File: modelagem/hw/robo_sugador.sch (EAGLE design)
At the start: 34 parts, among them M1 Roda esquerda, M2 Roda direita, M3 Sugador, M4 Servo

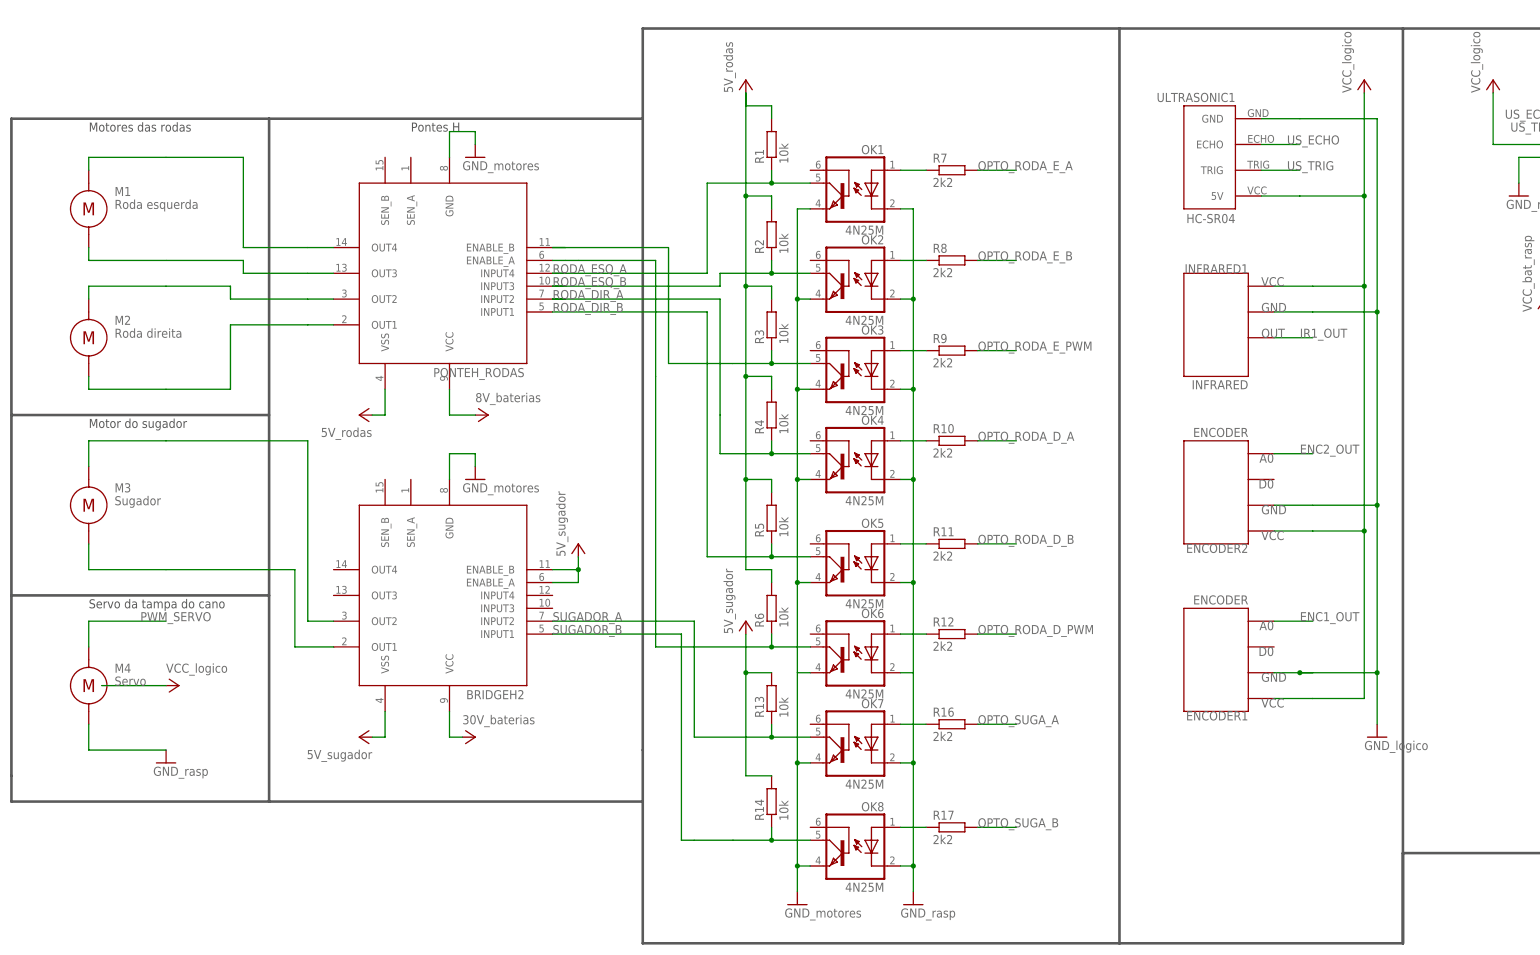
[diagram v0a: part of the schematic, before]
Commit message: Atualiza esquematico de hw e suas figuras
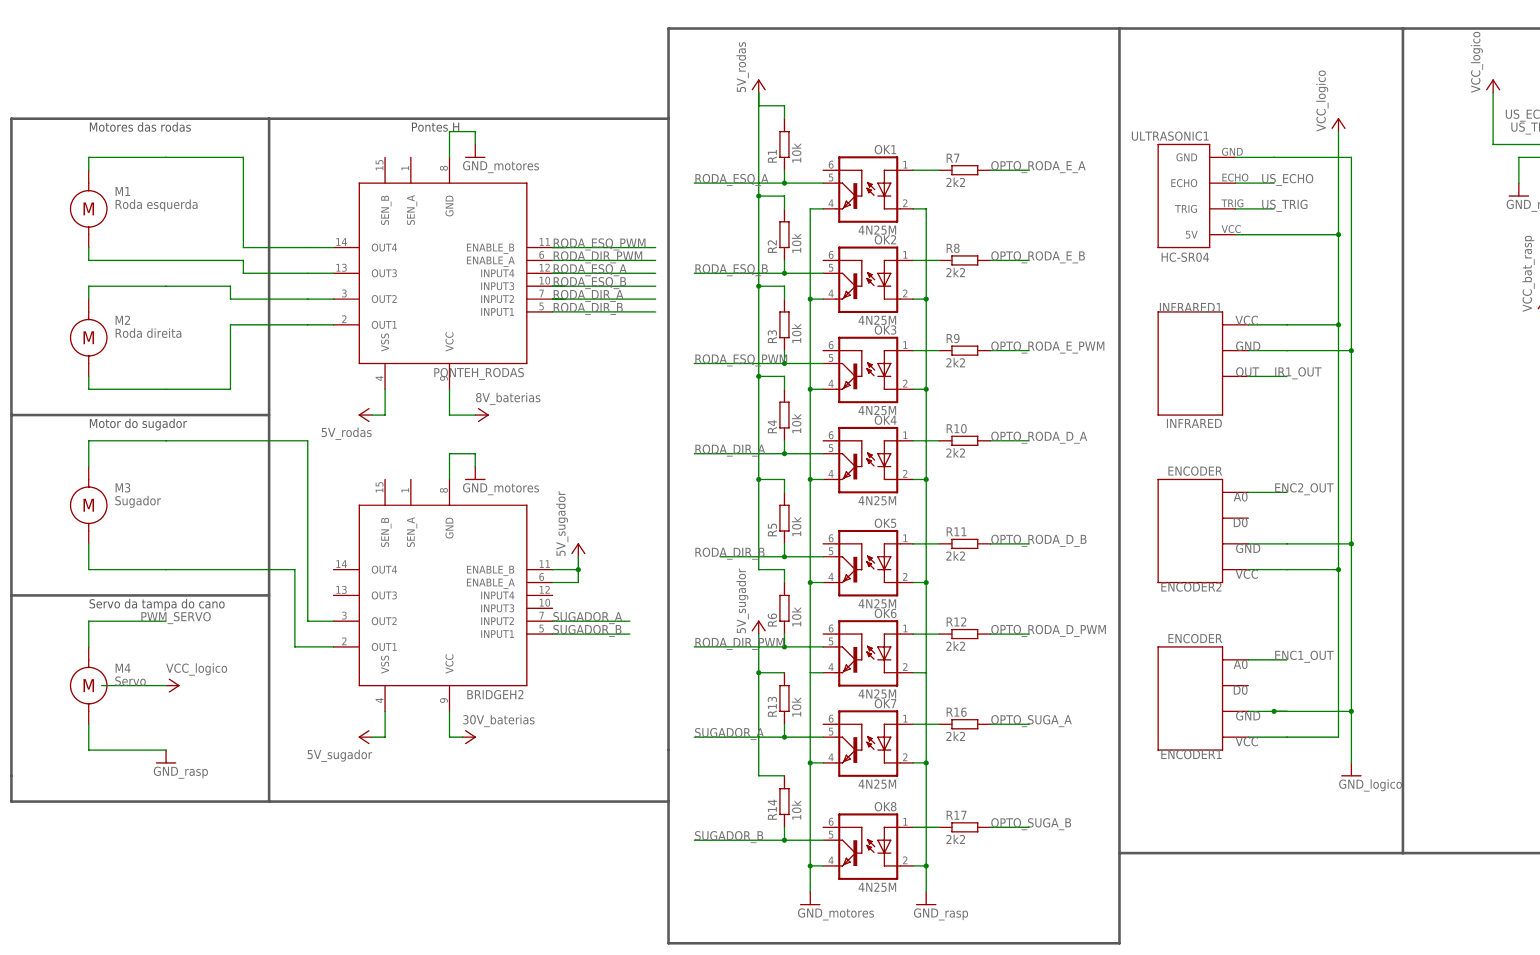
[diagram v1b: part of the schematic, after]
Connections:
- net N$6 renamed RODA_DIR_PWM
- net N$7 renamed RODA_ESQ_PWM
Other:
- moved on the sheet: OK1, OK2, OK3, OK4, OK5, OK6, OK7, OK8, R1, R10, R11, R12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
